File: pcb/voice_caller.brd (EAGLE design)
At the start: 52.4 x 59.1 mm, 36 parts, among them IC1 PRO_MICRO, IC2 AT45DB321D-S, IC3 78L12SMD, K1 TQ2SA-L2-5V

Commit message: RC values added.
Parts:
- C1, C2, C3, C4, C6, C7: value (none) -> 100nF
- C5: value (none) -> 10nF
- R1: value (none) -> 4r7
- R12, R13: value (none) -> 220
- R2: value (none) -> 1k
- R3: value (none) -> 3k3
- R5: value (none) -> 100k
- R6: value (none) -> 470
- R7: value (none) -> 10k
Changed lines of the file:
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@@
 </autorouter>
 <elements>
-<element name="C1" library="rcl" package="C1206K" value="" x="37.823125" y="56.125625" rot="R180"/>
-<element name="C2" library="rcl" package="C1206K" value="" x="15.803696875" y="39.752528125"/>
+<element name="C1" library="rcl" package="C1206K" value="100nF" x="37.823125" y="56.125625" rot="R180"/>
+<element name="C2" library="rcl" package="C1206K" value="100nF" x="15.803696875" y="39.752528125"/>
 <element name="IC2" library="memory-atmel" package="SO08-8S2" value="AT45DB321D-S" x="27.18" y="35.015" rot="R90"/>
 <element name="CONN_MIC" library="con-tycoelectronics" package="RJ45-NO-SHIELD" value="RJ45-8L-B" x="16.19" y="55.19" rot="R270">
@@
 <attribute name="OC_FARNELL" value="1279843" x="16.04" y="15.19" size="1.778" layer="27" rot="R270" display="off"/>
 </element>
-<element name="C3" library="rcl" package="C1206K" value="" x="30.8375" y="50.88875" rot="R270"/>
+<element name="C3" library="rcl" package="C1206K" value="100nF" x="30.8375" y="50.88875" rot="R270"/>
 <element name="IC3" library="linear" package="SO08" value="78L12SMD" x="37.723125" y="50.885" rot="R270"/>
 <element name="IC1" library="SparkFun-Boards" package="SPARKFUN_PRO_MICRO" value="PRO_MICRO" x="27.2" y="35" rot="R90"/>
@@
 <attribute name="MPN" value="B3F-1000" x="56.2325" y="55.185625" size="1.778" layer="27" display="off"/>
 </element>
-<element name="C4" library="rcl" package="C1206K" value="" x="44.045" y="39.273125"/>
-<element name="R3" library="rcl" package="M1206" value="" x="44.1325" y="35.08375" rot="R180"/>
-<element name="C5" library="rcl" package="C1206K" value="" x="43.97375" y="31.194375" rot="R180"/>
+<element name="C4" library="rcl" package="C1206K" value="100nF" x="44.045" y="39.273125"/>
+<element name="R3" library="rcl" package="M1206" value="3k3" x="44.1325" y="35.08375" rot="R180"/>
+<element name="C5" library="rcl" package="C1206K" value="10nF" x="43.97375" y="31.194375" rot="R180"/>
 <element name="R4" library="rcl" package="RTRIMT93XB" value="" x="44.92625" y="20.0025" rot="R180"/>
-<element name="C6" library="rcl" package="C1206K" value="" x="49.291875" y="20.081875" rot="R270"/>
-<element name="R5" library="rcl" package="M1206" value="" x="47.8" y="11.668125" rot="R270"/>
-<element name="R6" library="rcl" package="M1206" value="" x="44.78375" y="11.668125" rot="R270"/>
-<element name="C7" library="rcl" package="C1206K" value="" x="19.446875" y="35.004375" rot="R270"/>
+<element name="C6" library="rcl" package="C1206K" value="100nF" x="49.291875" y="20.081875" rot="R270"/>
+<element name="R5" library="rcl" package="M1206" value="100k" x="47.8" y="11.668125" rot="R270"/>
+<element name="R6" library="rcl" package="M1206" value="470" x="44.78375" y="11.668125" rot="R270"/>
+<element name="C7" library="rcl" package="C1206K" value="100nF" x="19.446875" y="35.004375" rot="R270"/>
 <element name="K1" library="relay" package="TQ-SA" value="TQ2SA-L2-5V" x="35.004375" y="15.636875" rot="R270">
 <attribute name="OC_NEWARK" value="64K3202" x="35.004375" y="15.636875" size="1.778" layer="27" rot="R270" display="off"/>
@@
 </element>
 <element name="T1" library="transistor" package="SOT23-BEC" value="" x="37.465" y="59.055" rot="MR0"/>
-<element name="R1" library="rcl" package="M1206" value="" x="35.8775" y="53.6575" rot="MR90"/>
-<element name="R2" library="rcl" package="M1206" value="" x="39.37" y="52.26214375" rot="MR270"/>
-<element name="R7" library="rcl" package="M1206" value="" x="42.8625" y="53.6575" rot="MR270"/>
-<element name="R12" library="rcl" package="M1206" value="" x="34.525" y="32.125" rot="MR270"/>
-<element name="R13" library="rcl" package="M1206" value="" x="37.7" y="32.1375" rot="MR270"/>
+<element name="R1" library="rcl" package="M1206" value="4r7" x="35.8775" y="53.6575" rot="MR90"/>
+<element name="R2" library="rcl" package="M1206" value="1k" x="39.37" y="52.26214375" rot="MR270"/>
+<element name="R7" library="rcl" package="M1206" value="10k" x="42.8625" y="53.6575" rot="MR270"/>
+<element name="R12" library="rcl" package="M1206" value="220" x="34.525" y="32.125" rot="MR270"/>
+<element name="R13" library="rcl" package="M1206" value="220" x="37.7" y="32.1375" rot="MR270"/>
 <element name="JP2" library="pinhead" package="1X02" value="" x="48.6085875" y="55.188184375" rot="R270"/>
 <element name="JP3" library="pinhead" package="1X02" value="" x="48.5925" y="35.2125" rot="R270"/>

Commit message: Values adjusted.
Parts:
- C4: value 100nF -> 100uF
- R5: value 100k -> 4k7
- R6: value 470 -> NP
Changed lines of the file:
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@@
 <attribute name="MPN" value="B3F-1000" x="56.2325" y="55.185625" size="1.778" layer="27" display="off"/>
 </element>
-<element name="C4" library="rcl" package="C1206K" value="100nF" x="44.045" y="39.273125"/>
+<element name="C4" library="rcl" package="C1206K" value="100uF" x="44.045" y="39.273125"/>
 <element name="R3" library="rcl" package="M1206" value="3k3" x="44.1325" y="35.08375" rot="R180"/>
 <element name="C5" library="rcl" package="C1206K" value="10nF" x="43.97375" y="31.194375" rot="R180"/>
 <element name="R4" library="rcl" package="RTRIMT93XB" value="" x="44.92625" y="20.0025" rot="R180"/>
 <element name="C6" library="rcl" package="C1206K" value="100nF" x="49.291875" y="20.081875" rot="R270"/>
-<element name="R5" library="rcl" package="M1206" value="100k" x="47.8" y="11.668125" rot="R270"/>
-<element name="R6" library="rcl" package="M1206" value="470" x="44.78375" y="11.668125" rot="R270"/>
+<element name="R5" library="rcl" package="M1206" value="4k7" x="47.8" y="11.668125" rot="R270"/>
+<element name="R6" library="rcl" package="M1206" value="NP" x="44.78375" y="11.668125" rot="R270"/>
 <element name="C7" library="rcl" package="C1206K" value="100nF" x="19.446875" y="35.004375" rot="R270"/>
 <element name="K1" library="relay" package="TQ-SA" value="TQ2SA-L2-5V" x="35.004375" y="15.636875" rot="R270">

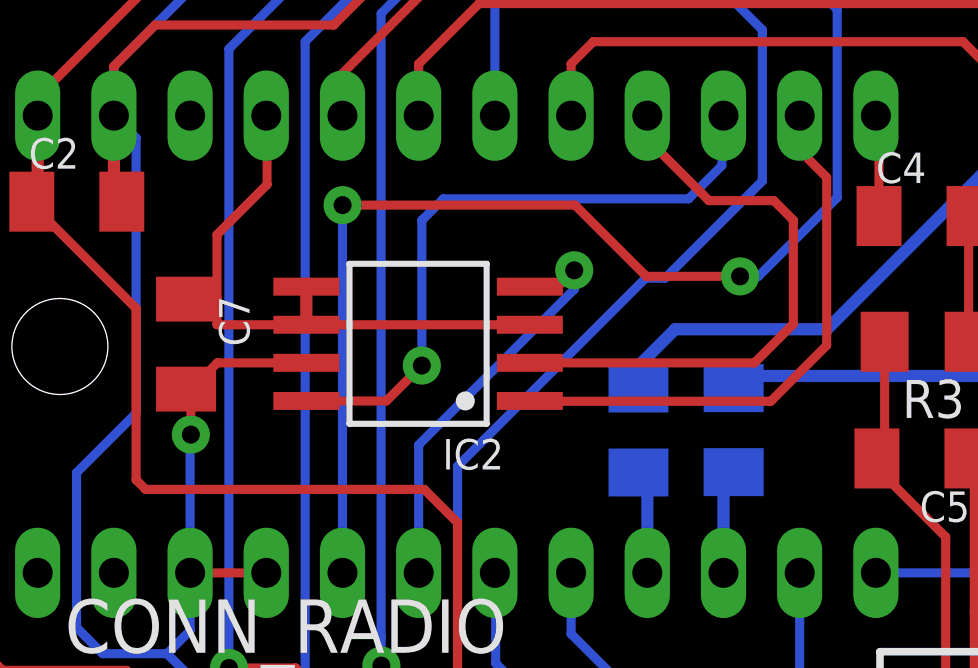
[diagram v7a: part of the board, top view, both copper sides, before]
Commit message: Flash IC replaced and almost routed.
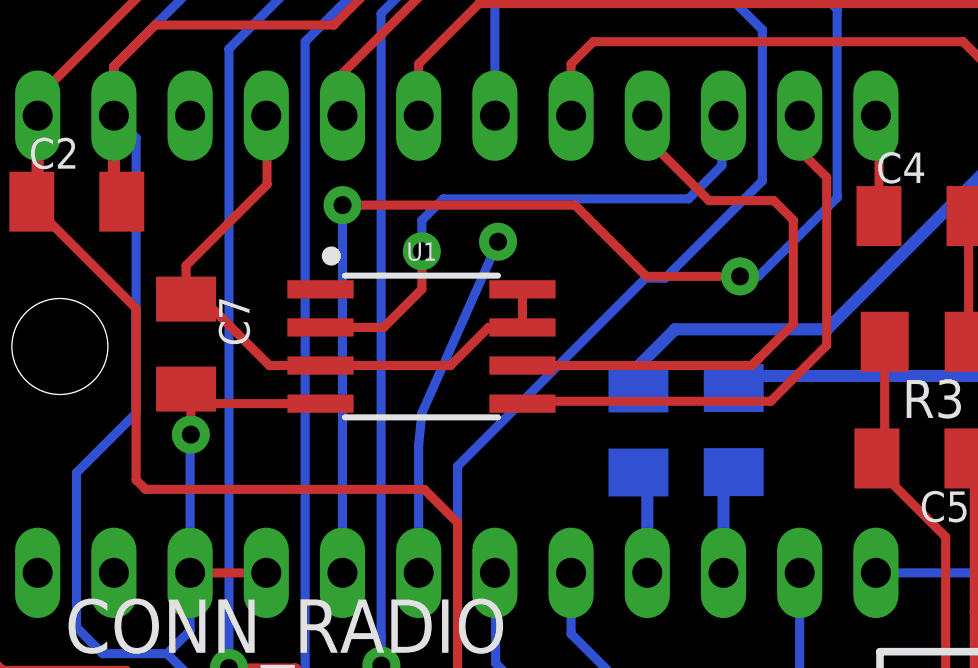
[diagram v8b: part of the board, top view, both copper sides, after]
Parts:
- removed IC2: AT45DB321D-S, memory-atmel:SO08-8S2
- added U1: 25F32006WSOI, SparkFun-IC-Memory:SO08-EIAJ
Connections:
- net +3V3: now also U1.3, U1.7, U1.8; no longer IC2.3, IC2.5, IC2.6
- net FLASH_CS: now also U1.1; no longer IC2.4
- net GND: now also U1.4; no longer IC2.7
- net MISO: now also U1.2; no longer IC2.8
- net MOSI: now also U1.5; no longer IC2.1
- net SCK: now also U1.6; no longer IC2.2
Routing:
- net MISO: track 21.6 -> 18.6 mm
- net FLASH_CS: track 14.2 -> 11.6 mm
- net +3V3: track 20.4 -> 21.2 mm
- net GND: track 271.2 -> 271.8 mm
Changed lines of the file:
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@@
 <element name="C1" library="rcl" package="C1206K" value="100nF" x="37.823125" y="56.125625" rot="R180"/>
 <element name="C2" library="rcl" package="C1206K" value="100nF" x="15.803696875" y="39.752528125"/>
-<element name="IC2" library="memory-atmel" package="SO08-8S2" value="AT45DB321D-S" x="27.18" y="35.015" rot="R90"/>
 <element name="CONN_MIC" library="con-tycoelectronics" package="RJ45-NO-SHIELD" value="RJ45-8L-B" x="16.19" y="55.19" rot="R270">
 <attribute name="OC_NEWARK" value="52K4445" x="16.19" y="55.19" size="1.778" layer="27" rot="R270" display="off"/>
@@
 <element name="JP2" library="pinhead" package="1X02" value="" x="48.6085875" y="55.188184375" rot="R270"/>
 <element name="JP3" library="pinhead" package="1X02" value="" x="48.5925" y="35.2125" rot="R270"/>
+<element name="U1" library="SparkFun-IC-Memory" package="SO08-EIAJ" value="25F32006WSOI" x="27.305" y="34.925" rot="R270">
+<attribute name="PROD_ID" value="IC-09109" x="27.305" y="34.925" size="1.778" layer="27" rot="R270" display="off"/>
+</element>
 </elements>
 <signals>
@@
 <contactref element="C1" pad="2"/>
 <contactref element="C2" pad="2"/>
-<contactref element="IC2" pad="7"/>
 <contactref element="C3" pad="2"/>
 <contactref element="CONN_MIC" pad="7"/>
@@
 <contactref element="S2" pad="3"/>
 <contactref element="S2" pad="4"/>
-<wire x1="23.455" y1="34.38" x2="20.489375" y2="34.38" width="0.3048" layer="1"/>
-<wire x1="20.489375" y1="34.38" x2="19.52625" y2="33.416875" width="0.3048" layer="1"/>
 <wire x1="22.12" y1="27.38" x2="19.58" y2="27.38" width="0.3048" layer="1"/>
 <contactref element="CONN_RADIO" pad="7"/>
@@
 <wire x1="17.78" y1="32.7025" x2="15.795625" y2="30.718125" width="0.3048" layer="16"/>
 <wire x1="15.795625" y1="30.718125" x2="15.795625" y2="25.55875" width="0.3048" layer="16"/>
+<contactref element="U1" pad="4"/>
+<wire x1="23.9268" y1="33.02" x2="19.446875" y2="33.02" width="0.3048" layer="1"/>
+<wire x1="19.446875" y1="33.02" x2="19.446875" y2="33.504375" width="0.4064" layer="1"/>
 </signal>
 <signal name="MOSI">
-<contactref element="IC2" pad="1"/>
 <contactref element="IC1" pad="14"/>
-<wire x1="30.915625" y1="33.099375" x2="30.905" y2="33.11" width="0.3048" layer="1"/>
 <wire x1="39.9" y1="42.62" x2="39.9" y2="42.1625" width="0.3048" layer="1"/>
 <wire x1="30.915625" y1="33.099375" x2="38.936875" y2="33.099375" width="0.3048" layer="1"/>
@@
 <wire x1="40.8" y1="40.5625" x2="39.9" y2="41.4625" width="0.3048" layer="1"/>
 <wire x1="39.9" y1="41.4625" x2="39.9" y2="42.62" width="0.3048" layer="1"/>
+<contactref element="U1" pad="5"/>
+<wire x1="30.6578" y1="33.02" x2="30.915625" y2="33.099375" width="0" layer="19" extent="1-1"/>
 </signal>
 <signal name="MISO">
-<contactref element="IC2" pad="8"/>
 <contactref element="IC1" pad="15"/>
 <wire x1="28.019375" y1="39.84625" x2="36.195" y2="39.84625" width="0.3048" layer="16"/>
@@
 <wire x1="37.30625" y1="40.9575" x2="37.30625" y2="42.56625" width="0.3048" layer="16"/>
 <wire x1="37.30625" y1="42.56625" x2="37.36" y2="42.62" width="0.3048" layer="16"/>
-<wire x1="23.455" y1="33.11" x2="26.125" y2="33.11" width="0.3048" layer="1"/>
-<wire x1="26.125" y1="33.11" x2="27.305" y2="34.29" width="0.3048" layer="1"/>
-<via x="27.305" y="34.29" extent="1-16" drill="0.6" diameter="1.27" shape="square"/>
-<wire x1="27.305" y1="34.29" x2="27.305" y2="39.131875" width="0.3048" layer="16"/>
+<via x="27.305" y="38.1" extent="1-16" drill="0.6" diameter="1.27" shape="square"/>
+<wire x1="27.305" y1="38.1" x2="27.305" y2="39.131875" width="0.3048" layer="16"/>
 <wire x1="27.305" y1="39.131875" x2="28.019375" y2="39.84625" width="0.3048" layer="16"/>
+<contactref element="U1" pad="2"/>
+<wire x1="23.9268" y1="35.56" x2="26.035" y2="35.56" width="0.3048" layer="1"/>
+<wire x1="26.035" y1="35.56" x2="27.305" y2="36.83" width="0.3048" layer="1"/>
+<wire x1="27.305" y1="36.83" x2="27.305" y2="38.1" width="0.3048" layer="1"/>
 </signal>
 <signal name="SCK">
-<contactref element="IC2" pad="2"/>
 <contactref element="IC1" pad="16"/>
-<wire x1="30.905" y1="34.38" x2="38.3925" y2="34.38" width="0.3048" layer="1"/>
-<wire x1="38.3925" y1="34.38" x2="39.6875" y2="35.675" width="0.3048" layer="1"/>
+<wire x1="38.3925" y1="34.38" x2="38.51875" y2="34.50625" width="0.3048" layer="1"/>
+<wire x1="38.51875" y1="34.50625" x2="39.6875" y2="35.675" width="0.3048" layer="1"/>
 <wire x1="39.6875" y1="35.675" x2="39.6875" y2="39.1375" width="0.3048" layer="1"/>
 <wire x1="39.6875" y1="39.1375" x2="39.0375" y2="39.7875" width="0.3048" layer="1"/>
@@
 <wire x1="34.8" y1="41.8625" x2="34.8" y2="42.6" width="0.3048" layer="1"/>
 <wire x1="34.8" y1="42.6" x2="34.82" y2="42.62" width="0.3048" layer="1"/>
+<contactref element="U1" pad="6"/>
+<wire x1="30.6578" y1="34.29" x2="38.3025" y2="34.29" width="0.3048" layer="1"/>
+<wire x1="38.3025" y1="34.29" x2="38.51875" y2="34.50625" width="0.3048" layer="1"/>
 </signal>
 <signal name="FLASH_CS">
-<contactref element="IC2" pad="4"/>
 <contactref element="IC1" pad="6"/>
-<via x="32.385" y="37.465" extent="1-16" drill="0.6" diameter="1.27" shape="square"/>
+<via x="29.845" y="38.4175" extent="1-16" drill="0.6" diameter="1.27" shape="square"/>
 <wire x1="27.2" y1="27.38" x2="27.2" y2="31.645" width="0.3048" layer="16"/>
-<wire x1="27.2" y1="31.645" x2="32.385" y2="36.83" width="0.3048" layer="16"/>
-<wire x1="32.385" y1="36.83" x2="32.385" y2="37.465" width="0.3048" layer="16"/>
-<wire x1="30.905" y1="36.92" x2="30.7975" y2="37.0275" width="0.3048" layer="1"/>
-<wire x1="30.7975" y1="37.0275" x2="31.9475" y2="37.0275" width="0.3048" layer="1"/>
-<wire x1="31.9475" y1="37.0275" x2="32.385" y2="37.465" width="0.3048" layer="1"/>
+<wire x1="27.2" y1="31.645" x2="27.305" y2="32.7025" width="0.3048" layer="16"/>
+<wire x1="27.305" y1="32.7025" x2="29.845" y2="38.4175" width="0.3048" layer="16"/>
+<contactref element="U1" pad="1"/>
+<wire x1="27.305" y1="32.7025" x2="23.9268" y2="36.83" width="0" layer="19" extent="1-16"/>
 </signal>
 <signal name="PTT">
@@
 <signal name="+3V3">
 <contactref element="IC1" pad="21"/>
-<contactref element="IC2" pad="6"/>
-<wire x1="23.455" y1="35.65" x2="20.47875" y2="35.65" width="0.3048" layer="1"/>
-<wire x1="20.47875" y1="36.504375" x2="20.47875" y2="38.655625" width="0.3048" layer="1"/>
-<wire x1="20.47875" y1="38.655625" x2="22.145625" y2="40.3225" width="0.3048" layer="1"/>
+<wire x1="19.446875" y1="37.62375" x2="22.145625" y2="40.3225" width="0.3048" layer="1"/>
 <wire x1="22.145625" y1="40.3225" x2="22.145625" y2="42.594375" width="0.3048" layer="1"/>
 <wire x1="22.145625" y1="42.594375" x2="22.12" y2="42.62" width="0.3048" layer="1"/>
 <contactref element="C7" pad="1"/>
-<wire x1="19.446875" y1="36.504375" x2="20.47875" y2="36.504375" width="0.3048" layer="1"/>
-<wire x1="20.47875" y1="35.65" x2="20.47875" y2="36.504375" width="0.3048" layer="1"/>
-<contactref element="IC2" pad="3"/>
-<contactref element="IC2" pad="5"/>
-<wire x1="23.455" y1="35.65" x2="23.455" y2="36.92" width="0.4064" layer="1"/>
-<wire x1="30.905" y1="35.65" x2="23.455" y2="35.65" width="0.3048" layer="1"/>
+<contactref element="U1" pad="3"/>
+<contactref element="U1" pad="7"/>
+<contactref element="U1" pad="8"/>
+<wire x1="19.446875" y1="37.62375" x2="19.446875" y2="36.504375" width="0.3048" layer="1"/>
+<wire x1="23.9268" y1="34.29" x2="22.225" y2="34.29" width="0.3048" layer="1"/>
+<wire x1="22.225" y1="34.29" x2="20.0025" y2="36.5125" width="0.3048" layer="1"/>
+<wire x1="20.0025" y1="36.5125" x2="19.455" y2="36.5125" width="0.4064" layer="1"/>
+<wire x1="19.455" y1="36.5125" x2="19.446875" y2="36.504375" width="0.4064" layer="1"/>
+<wire x1="30.6578" y1="36.83" x2="30.6578" y2="35.56" width="0.3048" layer="1"/>
+<wire x1="23.9268" y1="34.29" x2="28.2575" y2="34.29" width="0.3048" layer="1"/>
+<wire x1="28.2575" y1="34.29" x2="29.5275" y2="35.56" width="0.3048" layer="1"/>
+<wire x1="29.5275" y1="35.56" x2="30.6578" y2="35.56" width="0.3048" layer="1"/>
 </signal>
 <signal name="N$6">
